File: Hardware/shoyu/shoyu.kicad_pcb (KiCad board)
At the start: 2 copper layers, 58 parts, among them J1 5/9V Connector, J2 24V Connector, J3 SHORI OUT, J4 GAMEN_OUT, J5 MAE OUT, J6 AUDIO IN, U1 TPA3255DDVR, U2 TSR 1-24120

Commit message: Shoyu: Layout complete
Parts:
- added H1: MountingHole, MountingHole:MountingHole_2mm, F.Cu at (95.8, 78.0)
- added H2: MountingHole, MountingHole:MountingHole_2mm, F.Cu at (95.8, 126.0)
- added H3: MountingHole, MountingHole:MountingHole_2mm, F.Cu at (202.5, 78.0)
- added H4: MountingHole, MountingHole:MountingHole_2mm, F.Cu at (203.0, 126.0)
- added LS1: Speaker, TerminalBlock_CUI:TerminalBlock_CUI_TB007-508-02_1x02_P5.08mm_Horizontal, F.Cu at (199.9, 102.0)
- C10, C8, C9: footprint Capacitor_SMD:C_0603_1608Metric_Pad1.08x0.95mm_HandSolder -> Capacitor_SMD:C_0603_1608Metric
- C27, C28, C29, C30: value 1uF -> 2.2uF; footprint Capacitor_SMD:C_0603_1608Metric_Pad1.08x0.95mm_HandSolder -> Capacitor_SMD:C_0603_1608Metric
- U2: footprint My Footprints:TSR1-SINGLE_TRP -> My Feet pics:TSR1-SINGLE_TRP
- moved C21 72.4 mm to (198.2, 86.3), turned to -90 degrees
- moved C18 68.1 mm to (194.2, 85.9), turned to 90 degrees
- moved J5 67.4 mm to (102.8, 108.8), turned to -90 degrees
- moved C15 67.1 mm to (195.5, 85.9), turned to 90 degrees
- moved C22 66.5 mm to (198.6, 117.4), turned to -90 degrees
- moved C17 63.8 mm to (195.8, 117.4), turned to 90 degrees
- moved J2 63.6 mm to (124.5, 119.1)
- moved C16 62.8 mm to (194.5, 117.4), turned to 90 degrees
- moved C20 59.4 mm to (197.2, 117.0), turned to 90 degrees
- moved C19 56.1 mm to (196.8, 86.1), turned to 90 degrees
- moved J1 55.9 mm to (109.4, 118.9)
- moved J4 53.5 mm to (102.7, 96.3), turned to -90 degrees
- moved C26 44.7 mm to (175.1, 95.8), turned to 90 degrees
- moved C31 44.5 mm to (175.0, 106.5), turned to -90 degrees
- moved C32 44.3 mm to (161.0, 114.8), turned to -90 degrees
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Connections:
- C6 pad 1: Net-(J6-Pin_2) -> Net-(J6-Pin_1)
- C7 pad 1: Net-(J6-Pin_1) -> Net-(J6-Pin_2)
- J1 pad 2: +5V -> +9V
- J1 pad 4: +9V -> +5V
- U10 pad 1: Net-(J6-Pin_2) -> Net-(J6-Pin_1)
- U9 pad 2: Net-(J6-Pin_1) -> Net-(J6-Pin_2)
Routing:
- added copper zone on B.Cu, net GND
- added copper zone on F.Cu, net GND
- added copper zone on In1.Cu, net GND
- added copper zone on In2.Cu, net GND
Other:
- board outline added: 113.2 x 54 mm
- copper layers 2 -> 4
- board text added: "SHOYU REV 1"

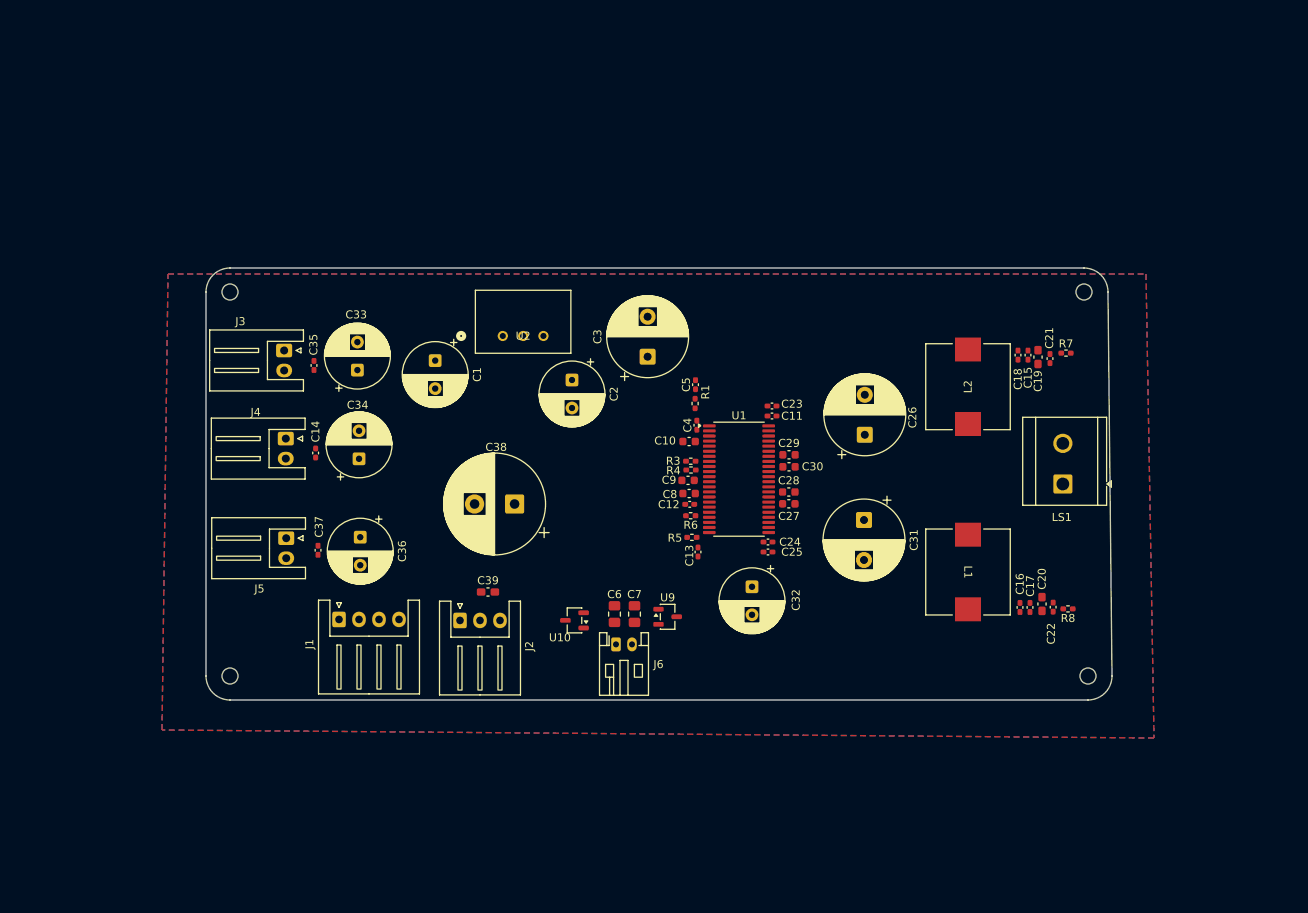
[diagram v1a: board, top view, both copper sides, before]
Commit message: Shoyu: Right side power zones finished.
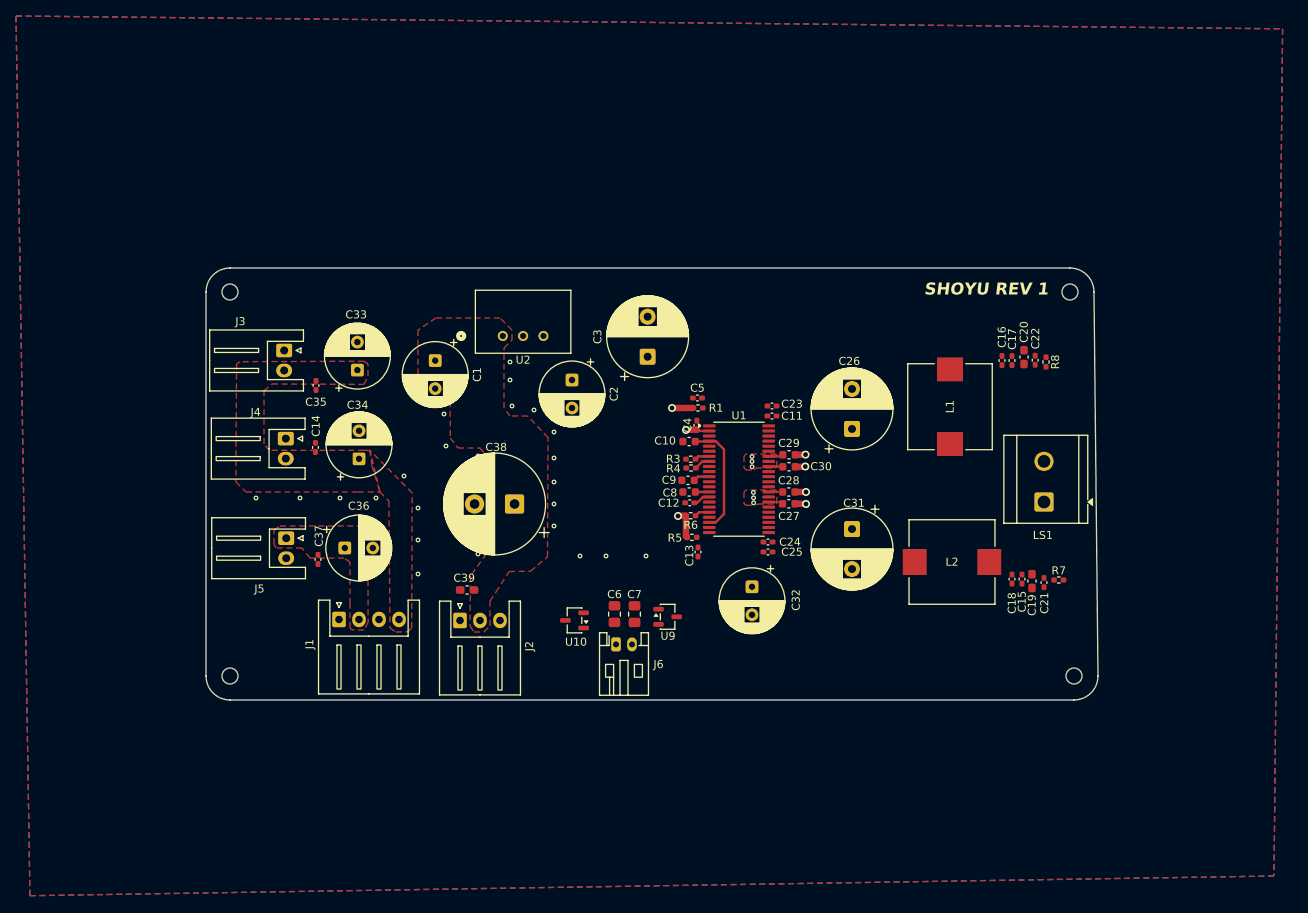
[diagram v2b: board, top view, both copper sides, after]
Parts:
- moved R8 31.0 mm to (197.8, 86.8), turned to -90 degrees
- moved C16 30.9 mm to (192.2, 86.6)
- moved C17 30.9 mm to (193.5, 86.6)
- moved C20 30.9 mm to (195.0, 86.1)
- moved C22 30.9 mm to (196.4, 86.5), turned to 90 degrees
- moved R7 28.4 mm to (199.3, 114.0)
- moved C15 28.0 mm to (194.8, 113.9)
- moved C18 28.0 mm to (193.5, 113.9)
- moved C19 28.0 mm to (196.0, 114.1)
- moved C21 28.0 mm to (197.5, 114.3), turned to 90 degrees
- moved L2 22.0 mm to (186.0, 111.8), turned to 0 degrees
- moved L1 20.8 mm to (185.8, 92.3), turned to 90 degrees
- moved LS1 3.26 mm to (197.5, 104.2)
- moved C39 2.62 mm to (125.4, 115.2), turned to 180 degrees
- moved C35 2.51 mm to (106.5, 89.7), turned to -90 degrees
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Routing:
- net /CHIP_M2: track 0.00 -> 14.4 mm
- net +12V: track 0.00 -> 9.41 mm, vias 0 -> 3
- net +24V: track 0.00 -> 7.19 mm, vias 0 -> 6
- net GND: track 0.00 -> 5.34 mm, vias 0 -> 30
- net Net-(U1-C_START): track 0.00 -> 2.18 mm
- net Net-(U1-DVDD): track 0.00 -> 2.07 mm
- net Net-(U1-FREQ_ADJ): track 0.00 -> 2.03 mm
- net Net-(U1-~{RESET}): track 0.00 -> 1.91 mm
- net Net-(U1-OC_ADJ): track 0.00 -> 1.87 mm
- net Net-(U1-AVDD): track 0.00 -> 1.75 mm
- added copper zone on In2.Cu, net +12V
- added copper zone on F.Cu, net +24V
- added copper zone on In2.Cu, net +24V
- added copper zone on F.Cu, net +5V
- added copper zone on F.Cu, net +9V
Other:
- board size 113.2 x 54 mm -> 111.5 x 54 mm

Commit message: Shoyu: rev 1 routing complete
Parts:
- moved C23 3.58 mm to (165.2, 95.4)
- moved C25 3.41 mm to (165.3, 108.0)
- moved U9 2.46 mm to (150.6, 121.0)
- moved R8 2.36 mm to (198.3, 84.5), turned to 180 degrees
- moved C31 2.22 mm to (171.8, 109.0)
- moved U10 2.01 mm to (138.6, 121.0)
- moved C26 1.95 mm to (171.8, 94.2)
- moved C16 1.50 mm to (192.2, 85.1)
- moved C17 1.50 mm to (193.5, 85.1)
- moved C22 1.50 mm to (196.4, 85.0)
- moved C20 1.14 mm to (195.0, 85.0)
- moved C11 1.00 mm to (162.5, 93.5), turned to 180 degrees
- moved R7 0.50 mm to (199.3, 114.5)
- moved C21 0.41 mm to (197.2, 114.0)
- moved C29 0.35 mm to (165.6, 98.0)
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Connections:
- net Net-(U1-INPUT_A) renamed /AUDIO_IN+
- net Net-(U1-INPUT_B) renamed /AUDIO_IN-
- net Net-(U1-OUT_A_39) renamed /INDUCTOR_IN_L2
- net Net-(U1-OUT_B) renamed /INDUCTOR_IN_L1
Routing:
- net /AUDIO_IN+: track 0.00 -> 27.4 mm
- net /AUDIO_IN-: track 0.00 -> 27.4 mm
- net GND: track 5.34 -> 31.2 mm, vias 30 -> 85
- net /INDUCTOR_IN_L1: track 0.00 -> 25.8 mm, vias 0 -> 2
- net /INDUCTOR_IN_L2: track 0.00 -> 25.0 mm, vias 0 -> 2
- net Net-(U1-~{RESET}): track 1.91 -> 14.1 mm, vias 0 -> 2
- net Net-(J6-Pin_1): track 0.00 -> 7.03 mm
- net Net-(J6-Pin_2): track 0.00 -> 6.27 mm
- net Net-(U1-GVDD_AB): track 0.00 -> 3.64 mm
- net Net-(U1-GVDD_CD): track 0.00 -> 3.16 mm
- net /BST_C: track 0.00 -> 1.91 mm
- net /BST_B: track 0.00 -> 1.59 mm
- net /BST_D: track 0.00 -> 1.57 mm
- net Net-(C21-Pad1): track 0.00 -> 1.53 mm
- net Net-(C22-Pad2): track 0.00 -> 1.32 mm
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- added copper zone on F.Cu, net /INDUCTOR_IN_L1
- added copper zone on F.Cu, net /INDUCTOR_IN_L2
- added copper zone on F.Cu, net Net-(C15-Pad2)
- added copper zone on F.Cu, net Net-(C16-Pad1)

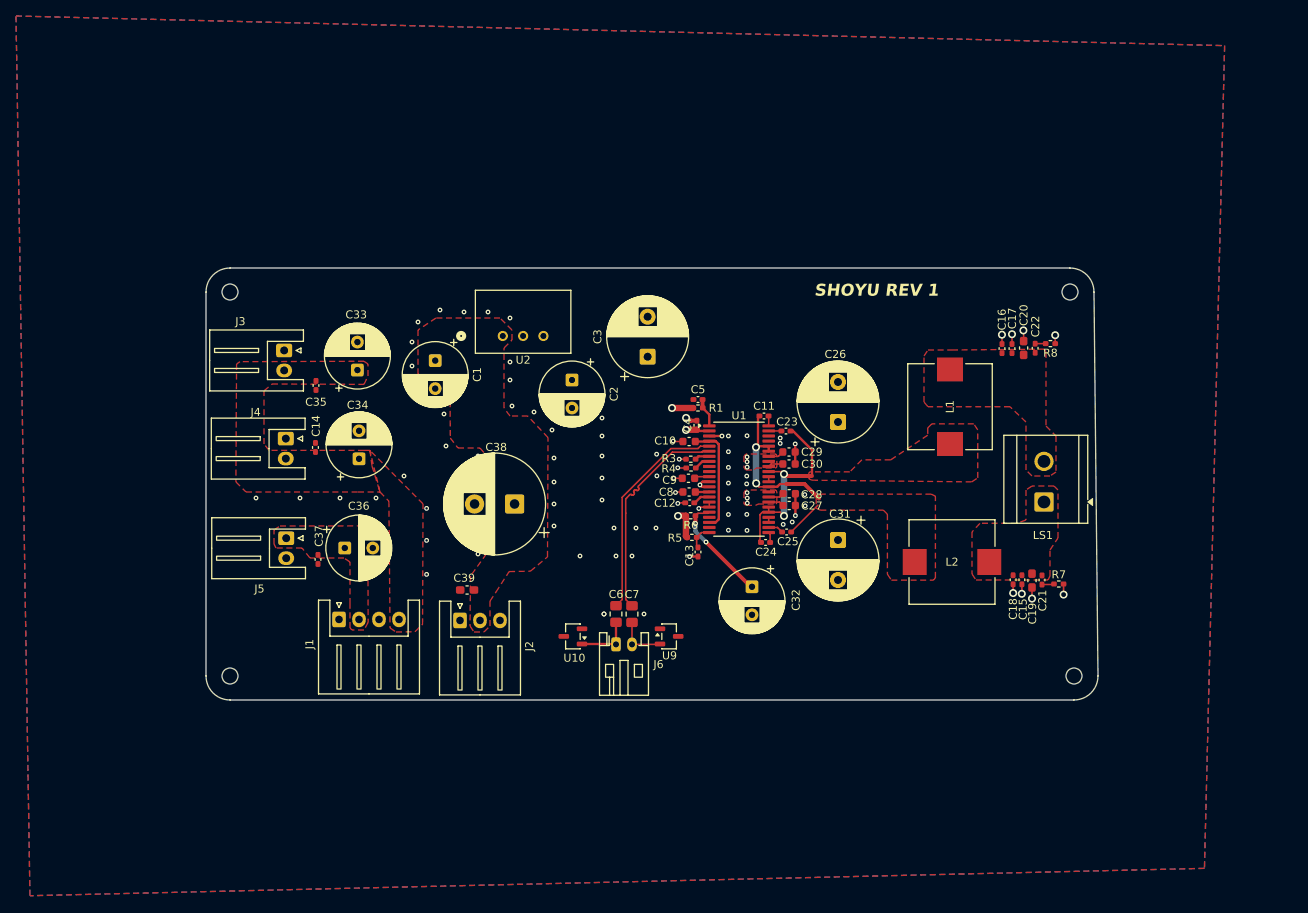
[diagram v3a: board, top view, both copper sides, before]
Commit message: Shoyu: New Film caps for output filter
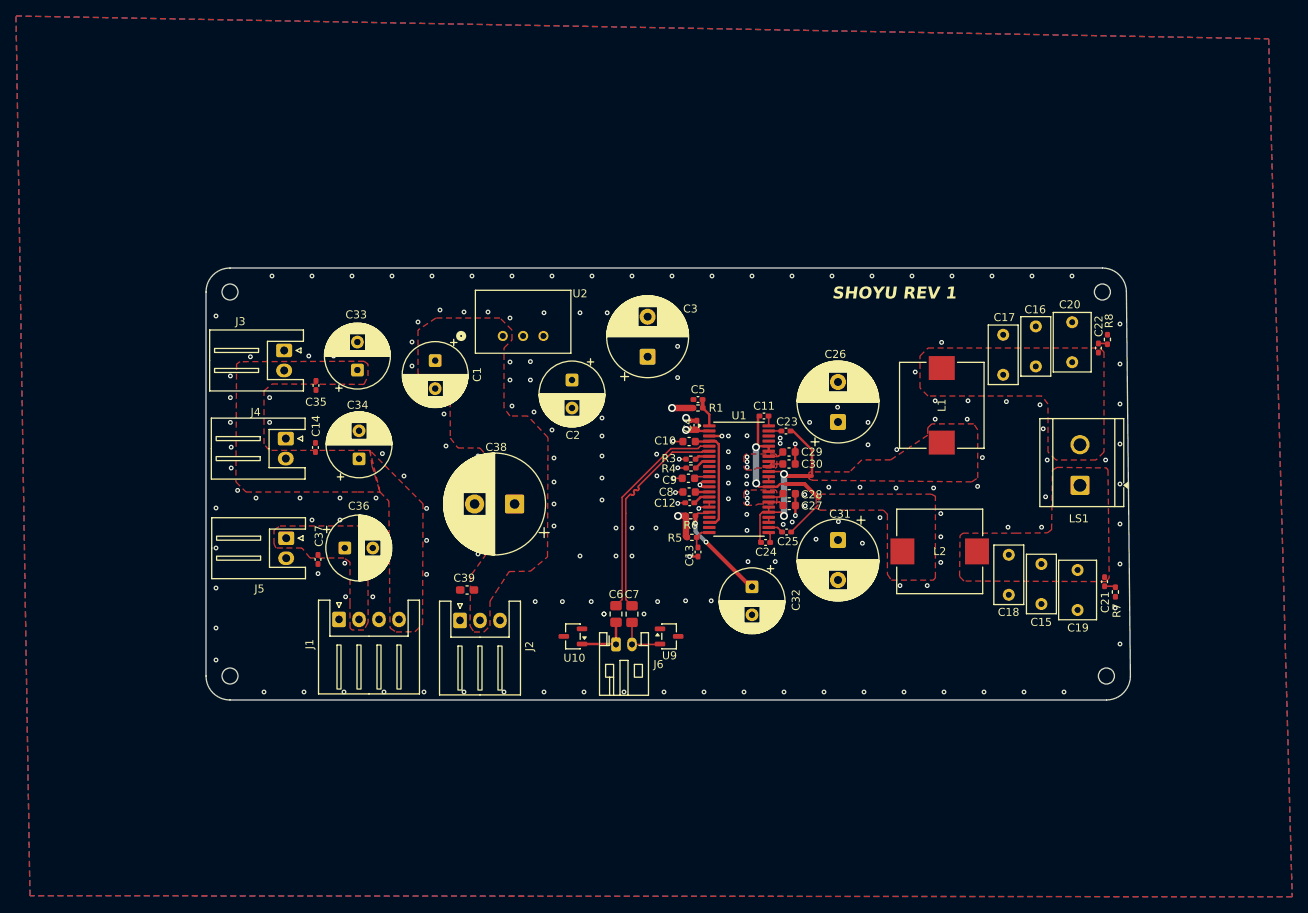
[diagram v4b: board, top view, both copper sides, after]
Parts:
- C15, C16, C17, C18: footprint Capacitor_SMD:C_0402_1005Metric_Pad0.74x0.62mm_HandSolder -> Capacitor_THT:C_Rect_L7.2mm_W3.5mm_P5.00mm
- C19, C20: footprint Capacitor_SMD:C_0603_1608Metric_Pad1.08x0.95mm_HandSolder -> Capacitor_THT:C_Rect_L7.2mm_W4.5mm_P5.00mm
- moved C22 7.91 mm to (204.3, 85.0)
- moved C21 7.83 mm to (205.1, 114.2)
- moved R7 7.15 mm to (206.4, 115.5), turned to -90 degrees
- moved R8 7.15 mm to (205.4, 83.9), turned to -90 degrees
- moved C19 6.79 mm to (201.7, 117.8)
- moved C20 6.33 mm to (201.0, 86.8)
- moved LS1 4.96 mm to (202.0, 102.2)
- moved C16 4.78 mm to (196.5, 87.3)
- moved H3 4.05 mm to (204.8, 78.0)
- moved H4 4.05 mm to (205.3, 126.0)
- moved C15 3.89 mm to (197.2, 117.0)
- moved C17 3.46 mm to (192.4, 88.3)
- moved L2 2.03 mm to (184.5, 110.4)
- moved C18 1.95 mm to (193.1, 115.8)
- moved L1 1.04 mm to (184.7, 92.2)
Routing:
- net GND: track 31.2 -> 21.6 mm, vias 85 -> 201
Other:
- board size 111.5 x 54 mm -> 115.6 x 54 mm

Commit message: New Gallery Images for Reddit
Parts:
- added G***: LOGO, MyFootprints:logo, F.Cu at (168.8, 77.0)
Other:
- board text added: "ARNAV"
- board text added: "WAVE FORGE"
